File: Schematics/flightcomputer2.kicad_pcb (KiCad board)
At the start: 4 copper layers, 80 x 80 mm, 86 parts, among them J1 Microsemi_FlashPro-JTAG-10, J2 Pyro, J3 USB_C_Receptacle, J4 Pyro, J5 Conn_01x05_Pin, J6 Conn_01x05_Pin, J7 Conn_Coaxial_Small, J8 Micro_SD_Card, Q1 BSC098N10NS5, Q2 BSC098N10NS5, Q3 BC817, U1 STM32F405RGT6, U2 SN65HVD230, U3 PowerIn, U4 LDL1117-3.3, U5 RFM95W-915S2, U6 MPL3115A2R1, U7 LSM6DS3TR-C, U8 W25Q128JVP, U9 H3LIS100DL, Y1 8mhz

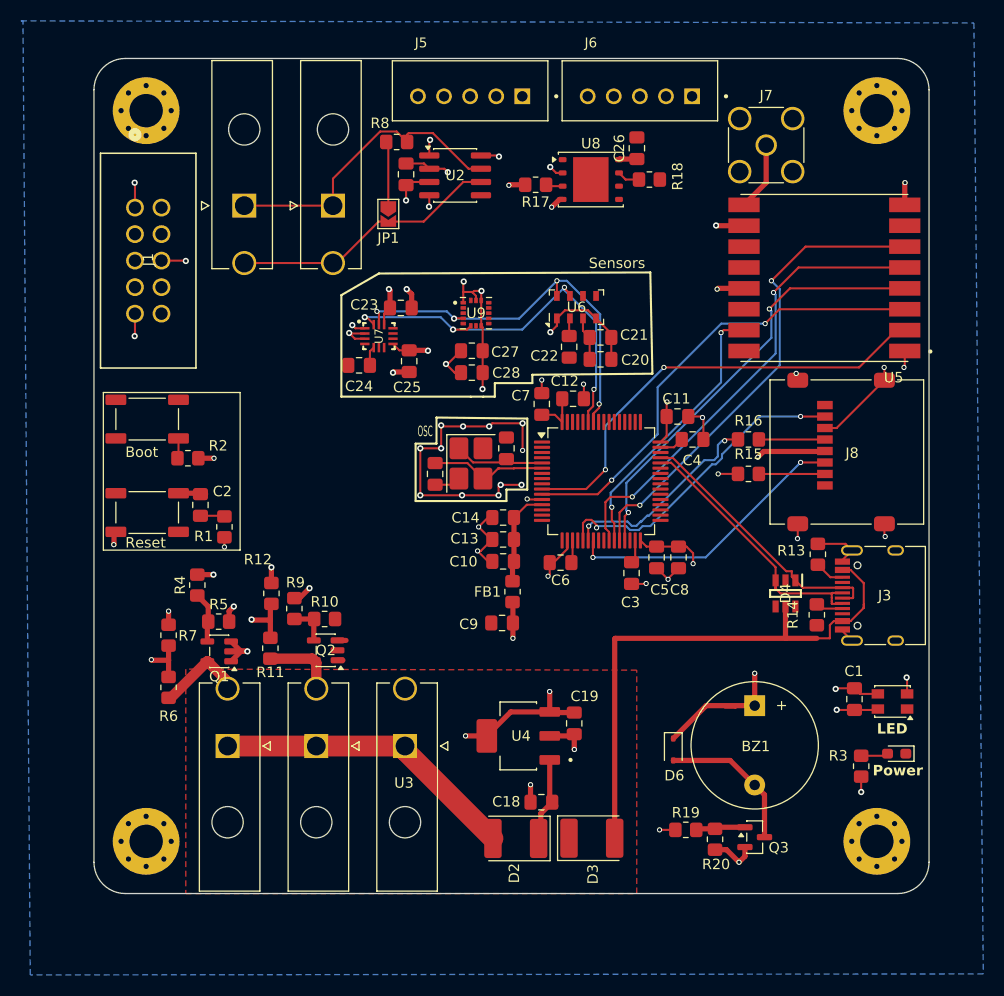
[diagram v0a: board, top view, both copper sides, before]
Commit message: finished routing pending final review
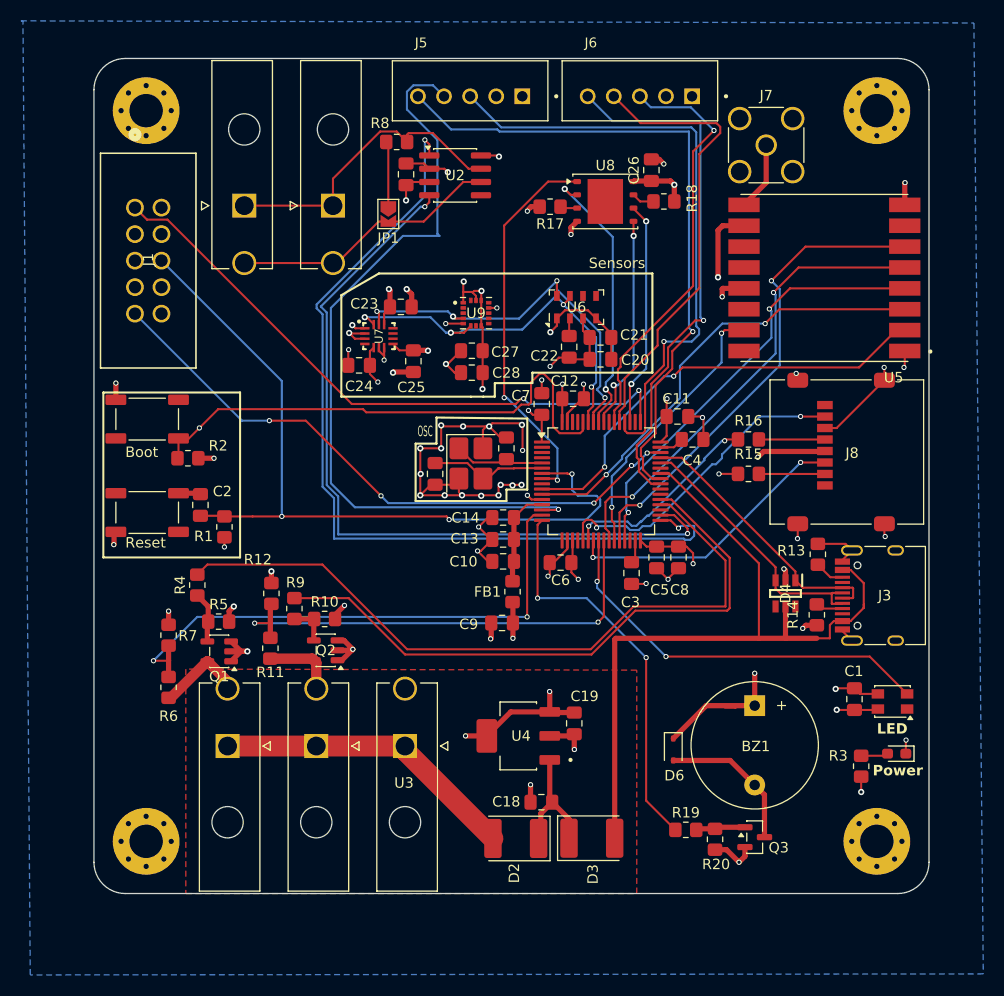
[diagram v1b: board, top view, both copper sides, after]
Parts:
- moved C26 2.52 mm to (168.4, 58.7)
- moved U8 2.52 mm to (164.0, 61.7)
- moved R17 2.52 mm to (158.7, 62.2)
- moved R18 2.52 mm to (169.6, 61.7)
- moved C25 0.40 mm to (145.6, 77.0)
- moved C23 0.10 mm to (144.4, 71.8)
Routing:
- net /Can_transceiver/CAN_TX_2: track 1.53 -> 84.1 mm, vias 1 -> 2
- net /GPS/GPS1_RX: track 0.00 -> 73.8 mm, vias 0 -> 1
- net /Can_transceiver/CAN_RX_2: track 1.11 -> 74.8 mm, vias 1 -> 2
- net /MCU/NRST: track 4.67 -> 76.4 mm, vias 1 -> 3
- net /MCU/PyroIgnite: track 1.55 -> 68.9 mm, vias 1 -> 0
- net /GPS/RESET1: track 0.00 -> 64.1 mm, vias 0 -> 1
- net /GPS/GPS1_TX: track 0.00 -> 58.5 mm, vias 0 -> 1
- net /MCU/SWCLK: track 2.40 -> 60.1 mm, vias 1 -> 2
- net /MCU/SWDIO: track 2.16 -> 59.9 mm, vias 1 -> 5
- net /Drogue/DrougeIgnite: track 1.84 -> 59.5 mm, vias 1 -> 0
- net /GPS/RESET2: track 0.00 -> 51.1 mm, vias 0 -> 1
- net /MCU/BOOT0: track 1.94 -> 50.4 mm, vias 0 -> 1
- net /MCU/PyroADC: track 4.67 -> 52.8 mm, vias 1 -> 2
- net /GPS/GPS2_RX: track 0.00 -> 43.7 mm
- net /Drogue/DrougeADC: track 5.11 -> 45.8 mm, vias 1 -> 2
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
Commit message: Updated PCB
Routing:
- net /MCU/SWCLK: track 60.1 -> 66.5 mm
- net /MCU/NRST: track 76.4 -> 71.1 mm
- net /MCU/SWDIO: track 59.9 -> 64.6 mm
- net /GPS/GPS1_RX: track 73.8 -> 71.6 mm
- net /Can_transceiver/CANH: track 29.7 -> 30.7 mm
- net /FlashMemory/SPI_MISO: track 26.6 -> 25.7 mm
- net /FlashSd/SDMOSI: track 30.6 -> 29.6 mm
- net /Accelerometer/AccelerometerSCL: track 39.0 -> 38.3 mm
- net /MCU/D-: track 25.9 -> 26.4 mm
- net /MCU/BOOT0: track 50.4 -> 50.1 mm, vias 1 -> 0
- net GND: track 171.1 -> 171.4 mm, vias 62 -> 77

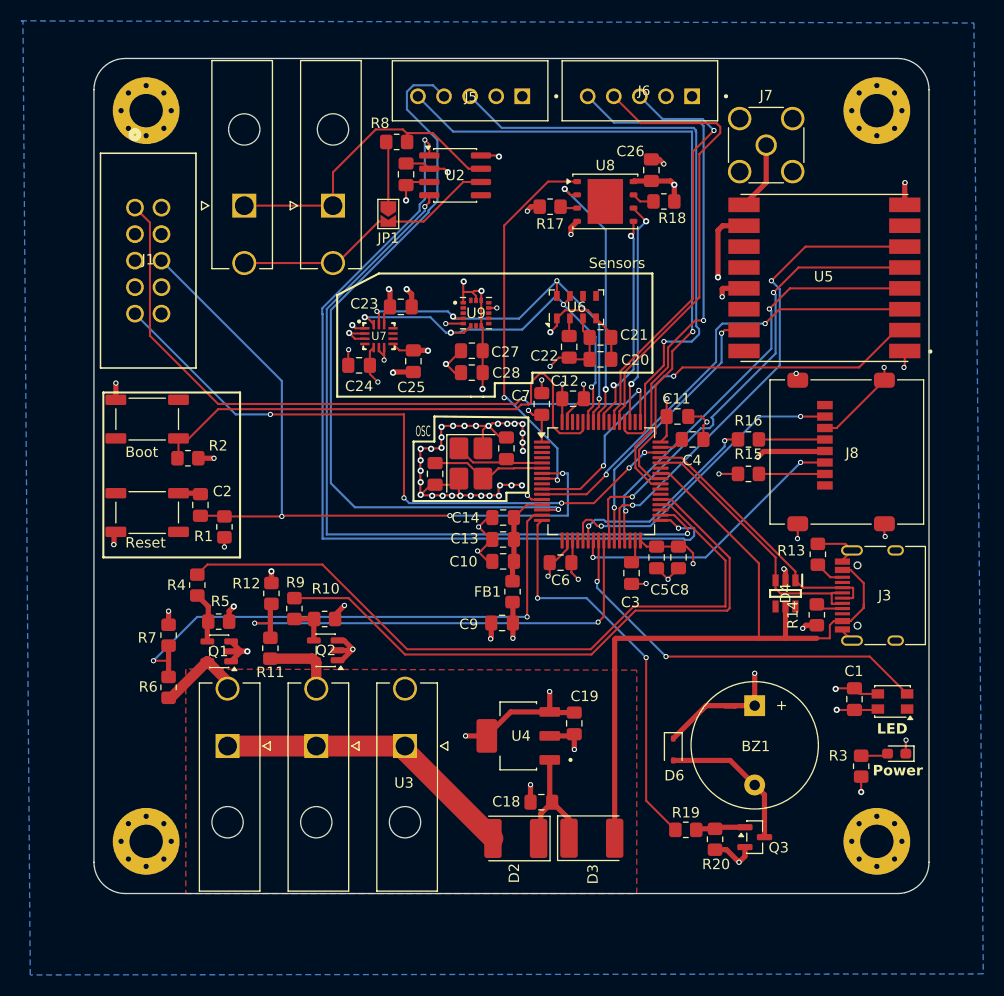
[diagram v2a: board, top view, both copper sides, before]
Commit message: fixing DRC Warnings updated USBC footprint/schematic, did impedance matching for the trace from rfm95 to antenna connector fixed resistor on flash memeory
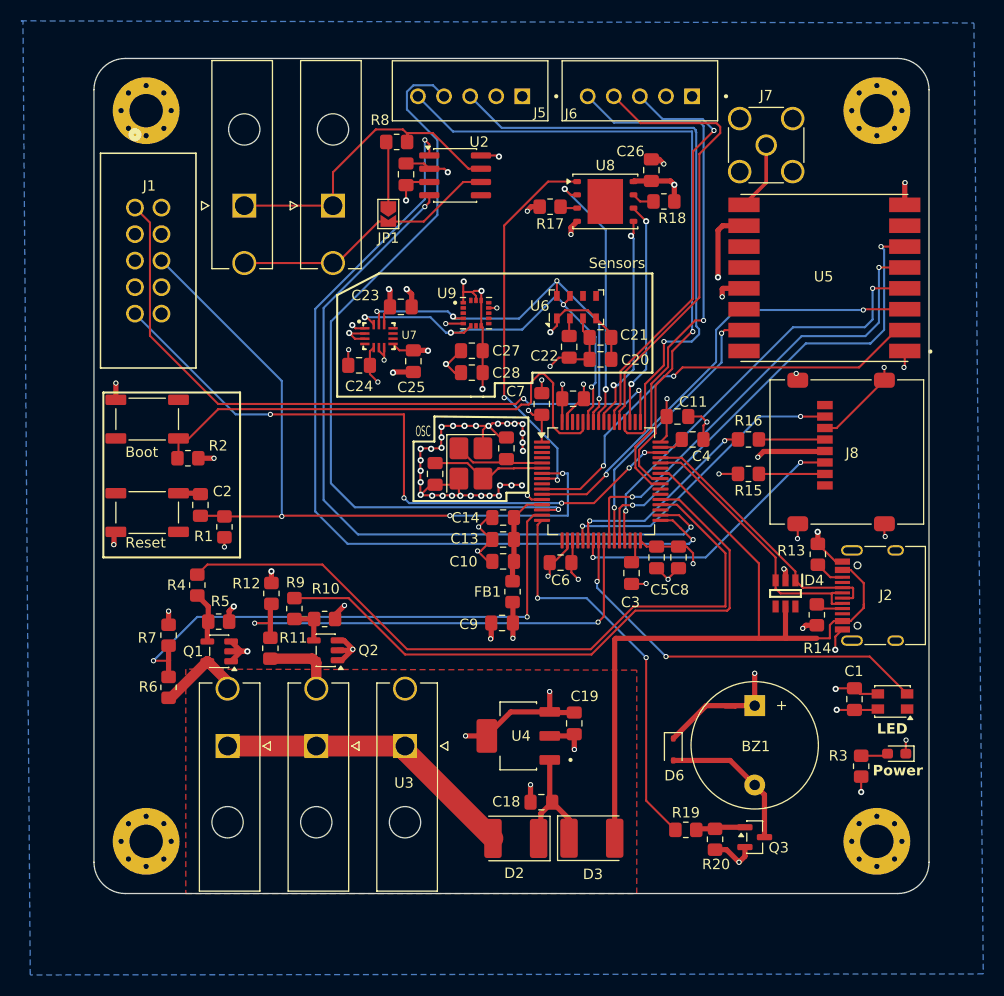
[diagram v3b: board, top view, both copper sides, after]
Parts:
- removed J3: USB_C_Receptacle, Connector_USB:USB_C_Receptacle_HRO_TYPE-C-31-M-12
- added J2: USB_C_Receptacle_USB2.0_16P, Connector_USB:USB_C_Receptacle_HRO_TYPE-C-31-M-12, F.Cu at (190.8, 99.5)
- C18: value 1u -> 100nf
- C19: value 4.7u -> 10u
- R16: value 220R -> 33R
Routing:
- net /LoRa/sxNSS: track 45.9 -> 44.6 mm
- net /Can_transceiver/CAN_RX_2: track 74.8 -> 73.6 mm
- net /LoRa/sxSCK: track 42.0 -> 41.1 mm
- net /Can_transceiver/CAN_TX_2: track 84.0 -> 83.2 mm
- net /LoRa/sxReset: track 46.7 -> 45.9 mm
- net GND: track 171.4 -> 171.7 mm, vias 77 -> 79
- added copper zone on F.Cu, net +3.3V
- removed copper zone on F.Cu, net (none)
